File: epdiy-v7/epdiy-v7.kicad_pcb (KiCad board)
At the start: 4 copper layers, 100 x 55 mm, 118 parts, among them J1 USB_C_Receptacle_USB2.0, J2 EXTENSION_HEADER, J3 USB_HDR, J4 XF2M-3315-1A, J5 CONN_BAT, J6 8BIT_HEADER, J7 ESP_HDR, Q1 AO3401A, Q3 MMBT3904, Q4 MMBT3904, U1 RT9080-33GJ5, U10 ED060XC5, U11 TP4056, U2 PCA9535PW, U3 RSL48_4P4X4P4, U4 USBLC6-2P6, U5 XC6206PxxxMR, U6 ED078KH6, U7 PCF8563T, U8 ESP32-S3-WROOM-1, U9 CH340C, Y1 32.768K

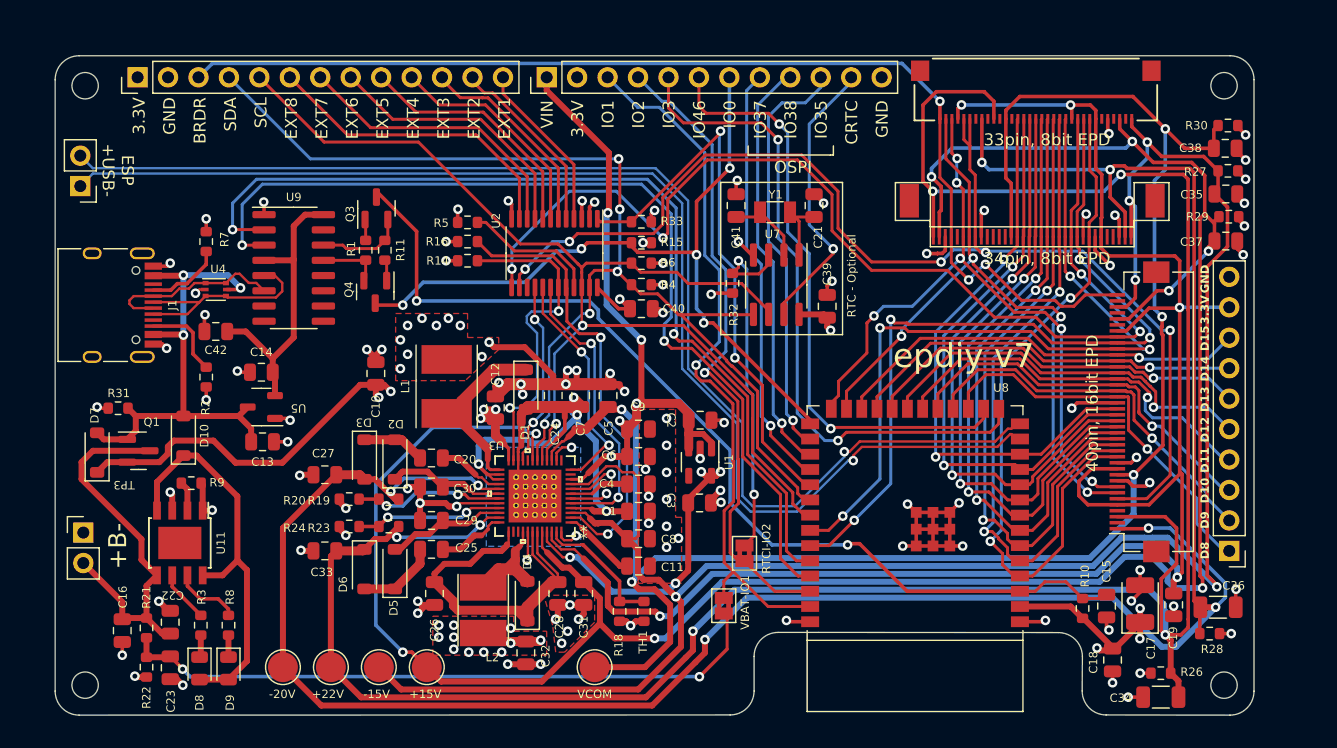
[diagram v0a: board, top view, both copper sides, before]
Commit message: Multiple changes. !!! Not for fabrication yet !!!
-USB-UART bridge removed-programming with USB only
-additional temperature and humidity sensor
-PCB layout modified - more consistent traces width, more 0.7/0.3 vias, teardrops etc
-jumpers removed and RX, TX signals routed to ext. pins
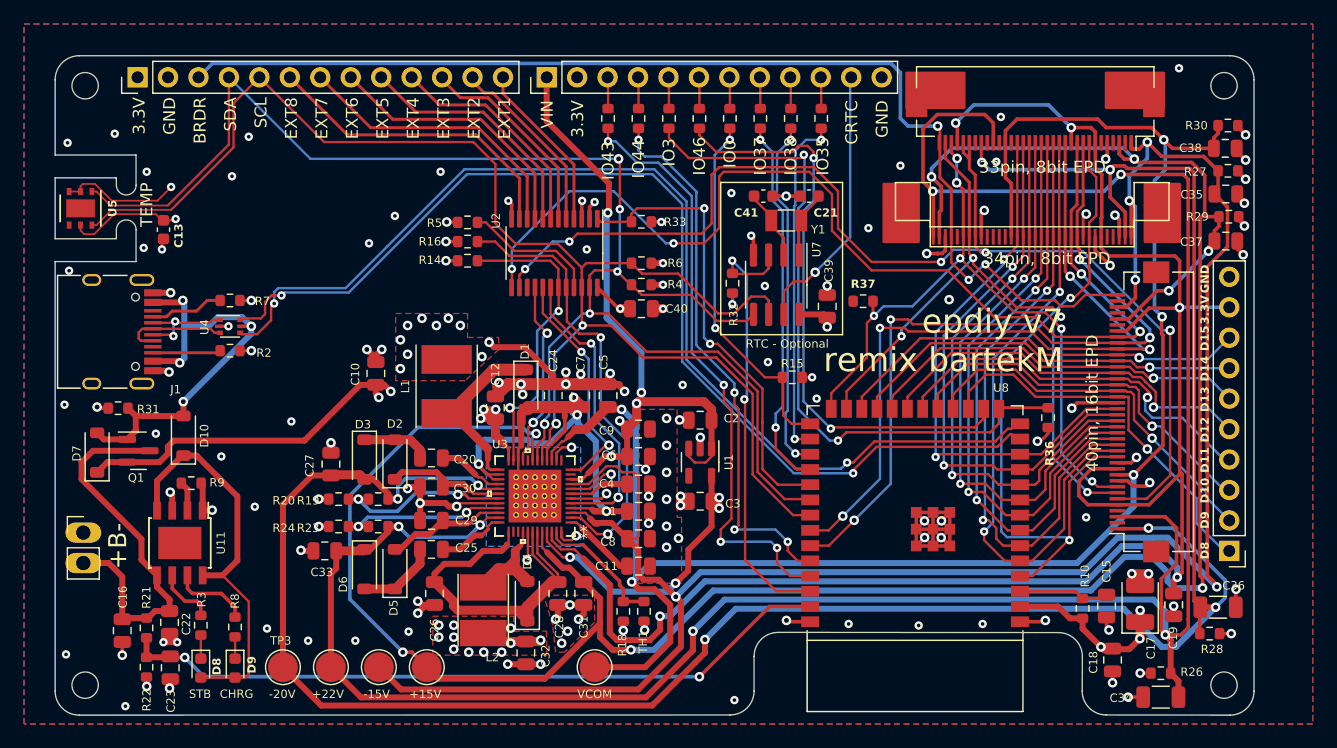
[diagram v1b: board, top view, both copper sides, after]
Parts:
- removed C14: 1uF, Capacitor_SMD:C_0805_2012Metric
- removed C42: 100nF, Capacitor_SMD:C_0805_2012Metric
- removed J3: USB_HDR, Connector_PinHeader_2.54mm:PinHeader_1x02_P2.54mm_Vertical
- removed JP1: VBAT_GPIO2, Jumper:SolderJumper-2_P1.3mm_Bridged2Bar_Pad1.0x1.5mm
- removed JP2: RTCINT_GPIO1, Jumper:SolderJumper-2_P1.3mm_Bridged2Bar_Pad1.0x1.5mm
- removed Q3, Q4: MMBT3904, Package_TO_SOT_SMD:SOT-23
- removed U9: CH340C, Package_SO:SOIC-16_3.9x9.9mm_P1.27mm
- added R12: 47R, Resistor_SMD:R_0603_1608Metric, F.Cu at (76.2, 14.7)
- added R13: 47R, Resistor_SMD:R_0603_1608Metric, F.Cu at (78.7, 14.7)
- added R17: 47R, Resistor_SMD:R_0603_1608Metric, F.Cu at (81.3, 14.7)
- added R25: 47R, Resistor_SMD:R_0603_1608Metric, F.Cu at (83.8, 14.7)
- added R34: 47R, Resistor_SMD:R_0603_1608Metric, F.Cu at (86.4, 14.7)
- added R35: 47R, Resistor_SMD:R_0603_1608Metric, F.Cu at (88.9, 14.7)
- added R36: 10k, Resistor_SMD:R_0603_1608Metric, F.Cu at (107.8, 39.7)
- added R37: 10k, Resistor_SMD:R_0603_1608Metric, F.Cu at (92.4, 30.0)
- C13: value 1uF -> 100nF; footprint Capacitor_SMD:C_0805_2012Metric -> Capacitor_SMD:C_0603_1608Metric
- C21, C41: footprint Capacitor_SMD:C_0805_2012Metric -> Capacitor_SMD:C_0603_1608Metric
- D8, D9: footprint LED_SMD:LED_0805_2012Metric -> LED_SMD:LED_0603_1608Metric
- J4: footprint epaper-breakout:CONN_ED097OC4 -> Connector_FFC-FPC:Hirose_FH12-33S-0.5SH_1x33-1MP_P0.50mm_Horizontal
- R1, R11: value 10k -> 47R
- R21: value 680k -> 510k
- R22: value 150k -> 100k
- U3: value RSL48_4P4X4P4 -> TPS651851RSLR
- U5: value XC6206PxxxMR -> HDC2080; footprint Package_TO_SOT_SMD:SOT-23-3 -> Package_SON:Texas_PWSON-N6
- moved R11 23.8 mm to (73.7, 14.7), turned to -90 degrees
- moved R1 23.0 mm to (71.1, 14.7)
- moved U5 22.4 mm to (27.1, 22.2), turned to -90 degrees
- moved C13 19.5 mm to (34.0, 24.0), turned to -90 degrees
- moved R15 16.9 mm to (86.5, 36.3)
- moved R7 5.30 mm to (39.6, 29.9), turned to 0 degrees
- moved U4 3.29 mm to (39.6, 32.1)
- moved R2 2.96 mm to (39.6, 34.1), turned to 0 degrees
- moved C41 2.41 mm to (84.1, 21.2), turned to 180 degrees
- moved J4 2.30 mm to (106.8, 14.9), turned to 180 degrees
- moved J1 2.22 mm to (29.1, 32.5)
- moved Y1 1.16 mm to (86.0, 23.2)
- moved C27 1.02 mm to (48.0, 43.6), turned to -90 degrees
- moved C21 0.89 mm to (87.9, 21.2), turned to 0 degrees
- moved R19 0.89 mm to (51.9, 46.5)
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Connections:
- C13 pad 1: GND -> 3.3V
- C13 pad 2: VBUS -> GND
- C23 pad 2: Net-(JP1-B) -> /GPIO_1
- J7 pad 10: /GPIO_35 -> Net-(J7-Pin_10)
- J7 pad 3: /GPIO_1 -> Net-(J7-Pin_3)
- J7 pad 4: /GPIO_2 -> Net-(J7-Pin_4)
- J7 pad 5: /GPIO_3 -> Net-(J7-Pin_5)
- J7 pad 6: /GPIO_46 -> Net-(J7-Pin_6)
- J7 pad 7: /IO0 -> Net-(J7-Pin_7)
- J7 pad 8: /GPIO_37 -> Net-(J7-Pin_8)
- J7 pad 9: /GPIO_36 -> Net-(J7-Pin_9)
- R1 pad 1: Net-(Q3-B) -> Net-(J7-Pin_3)
- R1 pad 2: /~{DTR} -> /GPIO_43
- R11 pad 1: Net-(Q4-B) -> Net-(J7-Pin_4)
- R11 pad 2: /~{RTS} -> /GPIO_44
- R21 pad 2: Net-(JP1-B) -> /GPIO_1
- R22 pad 1: Net-(JP1-B) -> /GPIO_1
- R32 pad 1: /RTC_INT -> /GPIO_2
- U5 pad 1: GND -> /SDA
- U5 pad 2: /UART_3.3V -> GND
- U5 pad 3: VBUS -> GND
- U7 pad 3: /RTC_INT -> /GPIO_2
- U8 pad 13: /ESP_USB- -> /USB_D-
- U8 pad 14: /ESP_USB+ -> /USB_D+
- U8 pad 36: /USB_TXD -> /GPIO_44
- U8 pad 37: /USB_RXD -> /GPIO_43
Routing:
- net /ESP_USB+: track 105.3 -> 0.00 mm, vias 1 -> 0
- net /ESP_USB-: track 105.3 -> 0.00 mm, vias 1 -> 0
- net /USB_D-: track 15.2 -> 99.3 mm, vias 0 -> 4
- net /USB_D+: track 18.0 -> 100.4 mm, vias 0 -> 2
- net /USB_RXD: track 79.8 -> 0.00 mm, vias 2 -> 0
- net /USB_TXD: track 79.2 -> 0.00 mm, vias 2 -> 0
- net /EN: track 82.2 -> 7.61 mm, vias 2 -> 0
- net Net-(JP1-B): track 54.8 -> 0.00 mm, vias 2 -> 0
- net /GPIO_43: track 0.00 -> 49.9 mm, vias 0 -> 4
- net /GPIO_44: track 0.00 -> 45.7 mm, vias 0 -> 4
- net /IO0: track 64.1 -> 30.1 mm, vias 5 -> 2
- net /RTC_INT: track 30.0 -> 0.00 mm, vias 2 -> 0
- net /SDA: track 98.2 -> 126.6 mm
- net /SCL: track 97.7 -> 124.1 mm
- net /UART_3.3V: track 25.1 -> 0.00 mm
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- added copper zone on B.Cu, net GND
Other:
- outline, holes or cut-outs redrawn
- board text added: "CHRG"
- board text added: "IO43"
- board text added: "IO44"
- board text added: "STB"
- board text added: "TEMP"
- board text added: "epdiy v7 by Valentin Roland 2023 remix by bartekM 2023 Thanks to the epdiy contributors! For sources and documentation visit https://github.com/vroland/epdiy https://github.com/bartekM-pl/"
- board text added: "epdiy v7 remix bartekM"
- board text removed: "ESP +USB-"
- board text removed: "IO1"
- board text removed: "IO2"
- board text removed: "OSPI"
- board text removed: "RTCI-IO2"
- board text removed: "VBAT-IO1"
- board text removed: "epdiy v7"
- board text removed: "epdiy v7 by Valentin Roland 2023 Thanks to the epdiy contributors! For sources and documentation visit https://github.com/vroland/epdiy"
